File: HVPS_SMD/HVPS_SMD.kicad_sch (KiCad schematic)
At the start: 17 parts

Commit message: Shrink
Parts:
- C1: value (none) -> 100uF; footprint (none) -> lib_fp:C_1210
- C2: value (none) -> 0.01uF
- C3: value (none) -> 0.22uF; footprint (none) -> lib_fp:C_1210
- Cc1: value (none) -> 22nF
- Cs1: value (none) -> 360pF
- J1, J2: value (none) -> CONN_01X02
- Q1: value (none) -> AO4294
- R1: footprint (none) -> lib_fp:R_0805
- Rc1: value (none) -> 4.7k; footprint (none) -> lib_fp:R_0805
- Rf1: value (none) -> 47k; footprint (none) -> lib_fp:R_0805
- Rs1: value (none) -> 249; footprint (none) -> lib_fp:R_1206
- Rs2: footprint (none) -> Resistor_SMD:R_1206_3216Metric
- T1: value (none) -> MagTop-HVSMPS; footprint (none) -> lib_fp:nixiemisc-WE-FLEX_ER11_5
- U1: value (none) -> LM3478SOIC8
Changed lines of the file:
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@@
       (effects (font (size 1.143 1.143)) (justify left bottom))
     )
-    (property "Value" "" (id 1) (at 111.76 101.6 0)
+    (property "Value" "LM3478SOIC8" (id 1) (at 111.76 101.6 0)
       (effects (font (size 1.143 1.143)) (justify left bottom))
     )
@@
       (effects (font (size 1.143 1.143)) (justify left bottom))
     )
-    (property "Value" "" (id 1) (at 146.05 85.09 0)
+    (property "Value" "AO4294" (id 1) (at 146.05 85.09 0)
       (effects (font (size 1.143 1.143)) (justify left bottom))
     )
@@
       (effects (font (size 1.27 1.27)) hide)
     )
-    (property "Value" "" (id 1) (at 109.22 113.03 0))
+    (property "Value" "GND" (id 1) (at 109.22 113.03 0))
     (property "Footprint" "" (id 2) (at 109.22 109.22 0))
     (property "Datasheet" "" (id 3) (at 109.22 109.22 0))
@@
       (effects (font (size 1.27 1.27)) hide)
     )
-    (property "Value" "" (id 1) (at 101.6 113.03 0))
+    (property "Value" "GND" (id 1) (at 101.6 113.03 0))
     (property "Footprint" "" (id 2) (at 101.6 109.22 0))
     (property "Datasheet" "" (id 3) (at 101.6 109.22 0))
@@
       (effects (font (size 1.27 1.27)) hide)
     )
-    (property "Value" "" (id 1) (at 143.51 113.03 0))
+    (property "Value" "GND" (id 1) (at 143.51 113.03 0))
     (property "Footprint" "" (id 2) (at 143.51 109.22 0))
     (property "Datasheet" "" (id 3) (at 143.51 109.22 0))
@@
       (effects (font (size 1.27 1.27)) (justify left))
     )
-    (property "Footprint" "" (id 2) (at 143.51 102.87 0)
-      (effects (font (size 1.27 1.27)) hide)
-    )
-    (property "Datasheet" "" (id 3) (at 143.51 102.87 0)
+    (property "Footprint" "Resistor_SMD:R_1206_3216Metric" (id 2) (at 143.51 102.87 0)
+      (effects (font (size 1.27 1.27)) hide)
+    )
+    (property "Datasheet" "C327069" (id 3) (at 143.51 102.87 0)
       (effects (font (size 1.27 1.27)) hide)
     )
@@
       (effects (font (size 1.27 1.27)) (justify left))
     )
-    (property "Value" "" (id 1) (at 137.414 104.902 0)
+    (property "Value" "0.01uF" (id 1) (at 137.414 104.902 0)
       (effects (font (size 1.27 1.27)) (justify left))
     )
@@
       (effects (font (size 1.27 1.27)) hide)
     )
-    (property "Value" "" (id 1) (at 137.16 113.03 0))
+    (property "Value" "GND" (id 1) (at 137.16 113.03 0))
     (property "Footprint" "" (id 2) (at 137.16 109.22 0))
     (property "Datasheet" "" (id 3) (at 137.16 109.22 0))
@@
       (effects (font (size 1.27 1.27)) (justify left))
     )
-    (property "Value" "" (id 1) (at 87.884 101.092 0)
+    (property "Value" "22nF" (id 1) (at 87.884 101.092 0)
       (effects (font (size 1.27 1.27)) (justify left))
     )
@@
       (effects (font (size 1.27 1.27)) (justify left))
     )
-    (property "Value" "" (id 1) (at 88.392 106.426 0)
-      (effects (font (size 1.27 1.27)) (justify left))
-    )
-    (property "Footprint" "" (id 2) (at 87.63 105.41 0)
+    (property "Value" "4.7k" (id 1) (at 88.392 106.426 0)
+      (effects (font (size 1.27 1.27)) (justify left))
+    )
+    (property "Footprint" "lib_fp:R_0805" (id 2) (at 87.63 105.41 0)
       (effects (font (size 1.27 1.27)) hide)
     )
@@
       (effects (font (size 1.27 1.27)) hide)
     )
-    (property "Value" "" (id 1) (at 87.63 113.03 0))
+    (property "Value" "GND" (id 1) (at 87.63 113.03 0))
     (property "Footprint" "" (id 2) (at 87.63 109.22 0))
     (property "Datasheet" "" (id 3) (at 87.63 109.22 0))
@@
       (effects (font (size 1.27 1.27)) (justify left))
     )
-    (property "Value" "" (id 1) (at 192.024 42.672 0)
-      (effects (font (size 1.27 1.27)) (justify left))
-    )
-    (property "Footprint" "" (id 2) (at 191.77 40.64 0)
+    (property "Value" "0.22uF" (id 1) (at 192.024 42.672 0)
+      (effects (font (size 1.27 1.27)) (justify left))
+    )
+    (property "Footprint" "lib_fp:C_1210" (id 2) (at 191.77 40.64 0)
       (effects (font (size 1.27 1.27)) hide)
     )
@@
       (effects (font (size 1.27 1.27)) hide)
     )
-    (property "Value" "" (id 1) (at 191.77 62.23 0))
+    (property "Value" "GND" (id 1) (at 191.77 62.23 0))
     (property "Footprint" "" (id 2) (at 191.77 58.42 0))
     (property "Datasheet" "" (id 3) (at 191.77 58.42 0))
@@
       (effects (font (size 1.27 1.27)) (justify left))
     )
-    (property "Value" "" (id 1) (at 88.646 85.598 0)
-      (effects (font (size 1.27 1.27)) (justify left))
-    )
-    (property "Footprint" "" (id 2) (at 87.63 86.36 0)
+    (property "Value" "47k" (id 1) (at 88.646 85.598 0)
+      (effects (font (size 1.27 1.27)) (justify left))
+    )
+    (property "Footprint" "lib_fp:R_0805" (id 2) (at 87.63 86.36 0)
       (effects (font (size 1.27 1.27)) hide)
     )
@@
       (effects (font (size 1.27 1.27)) hide)
     )
-    (property "Value" "" (id 1) (at 177.8 113.03 0))
+    (property "Value" "GND" (id 1) (at 177.8 113.03 0))
     (property "Footprint" "" (id 2) (at 177.8 109.22 0))
     (property "Datasheet" "" (id 3) (at 177.8 109.22 0))
@@
       (effects (font (size 1.27 1.27)) (justify left))
     )
-    (property "Value" "" (id 1) (at 131.572 70.866 0)
-      (effects (font (size 1.27 1.27)) (justify left))
-    )
-    (property "Footprint" "" (id 2) (at 130.81 69.85 0)
+    (property "Value" "249" (id 1) (at 131.572 70.866 0)
+      (effects (font (size 1.27 1.27)) (justify left))
+    )
+    (property "Footprint" "lib_fp:R_1206" (id 2) (at 130.81 69.85 0)
       (effects (font (size 1.27 1.27)) hide)
     )
@@
       (effects (font (size 1.27 1.27)) (justify left))
     )
-    (property "Value" "" (id 1) (at 131.064 62.992 0)
+    (property "Value" "360pF" (id 1) (at 131.064 62.992 0)
       (effects (font (size 1.27 1.27)) (justify left))
     )
@@
       (effects (font (size 1.27 1.27)) (justify left))
     )
-    (property "Value" "" (id 1) (at 69.215 90.17 0)
-      (effects (font (size 1.27 1.27)) (justify left))
-    )
-    (property "Footprint" "" (id 2) (at 68.58 87.63 0)
+    (property "Value" "100uF" (id 1) (at 69.215 90.17 0)
+      (effects (font (size 1.27 1.27)) (justify left))
+    )
+    (property "Footprint" "lib_fp:C_1210" (id 2) (at 68.58 87.63 0)
       (effects (font (size 1.27 1.27)) hide)
     )
@@
       (effects (font (size 1.27 1.27)) hide)
     )
-    (property "Value" "" (id 1) (at 68.58 113.03 0))
+    (property "Value" "GND" (id 1) (at 68.58 113.03 0))
     (property "Footprint" "" (id 2) (at 68.58 109.22 0))
     (property "Datasheet" "" (id 3) (at 68.58 109.22 0))
@@
     (in_bom yes) (on_board yes)
     (property "Reference" "J2" (id 0) (at 43.18 63.5 0))
-    (property "Value" "" (id 1) (at 40.64 59.69 90))
+    (property "Value" "CONN_01X02" (id 1) (at 40.64 59.69 90))
     (property "Footprint" "NixieClockMaster:Header_MA02-Edge" (id 2) (at 43.18 59.69 0)
       (effects (font (size 1.27 1.27)) hide)
@@
       (effects (font (size 1.27 1.27)) hide)
     )
-    (property "Value" "" (id 1) (at 43.18 99.06 0))
+    (property "Value" "GND" (id 1) (at 43.18 99.06 0))
     (property "Footprint" "" (id 2) (at 43.18 95.25 0))
     (property "Datasheet" "" (id 3) (at 43.18 95.25 0))
@@
       (effects (font (size 1.27 1.27)) hide)
     )
-    (property "Value" "" (id 1) (at 49.53 99.06 0))
+    (property "Value" "VCC" (id 1) (at 49.53 99.06 0))
     (property "Footprint" "" (id 2) (at 49.53 95.25 0))
     (property "Datasheet" "" (id 3) (at 49.53 95.25 0))
@@
       (effects (font (size 1.27 1.27)) hide)
     )
-    (property "Value" "" (id 1) (at 55.88 97.536 0))
+    (property "Value" "HT" (id 1) (at 55.88 97.536 0))
     (property "Footprint" "" (id 2) (at 55.88 95.25 0))
     (property "Datasheet" "" (id 3) (at 55.88 95.25 0))
@@
       (effects (font (size 1.27 1.27)) (justify left))
     )
-    (property "Footprint" "" (id 2) (at 177.8 76.2 0)
+    (property "Footprint" "lib_fp:R_0805" (id 2) (at 177.8 76.2 0)
       (effects (font (size 1.27 1.27)) hide)
     )
@@
     (in_bom yes) (on_board yes)
     (property "Reference" "J1" (id 0) (at 43.18 46.99 0))
-    (property "Value" "" (id 1) (at 40.64 43.18 90))
+    (property "Value" "CONN_01X02" (id 1) (at 40.64 43.18 90))
     (property "Footprint" "NixieClockMaster:Header_MA02-Edge" (id 2) (at 43.18 43.18 0)
       (effects (font (size 1.27 1.27)) hide)
@@
     (in_bom yes) (on_board yes)
     (property "Reference" "#FLG0101" (id 0) (at 109.22 42.799 0))
-    (property "Value" "" (id 1) (at 109.22 45.1104 0))
+    (property "Value" "PWR_FLAG" (id 1) (at 109.22 45.1104 0))
     (property "Footprint" "" (id 2) (at 109.22 49.53 0)
       (effects (font (size 1.27 1.27)) hide)
@@
     (in_bom yes) (on_board yes)
     (property "Reference" "#FLG0102" (id 0) (at 170.18 96.139 0))
-    (property "Value" "" (id 1) (at 170.18 98.4504 0))
+    (property "Value" "PWR_FLAG" (id 1) (at 170.18 98.4504 0))
     (property "Footprint" "" (id 2) (at 170.18 102.87 0)
       (effects (font (size 1.27 1.27)) hide)
@@
       (effects (font (size 1.27 1.27)) hide)
     )
-    (property "Value" "" (id 1) (at 205.74 23.5204 0))
+    (property "Value" "PWR_FLAG" (id 1) (at 205.74 23.5204 0))
     (property "Footprint" "" (id 2) (at 205.74 27.94 0)
       (effects (font (size 1.27 1.27)) hide)
@@
       (effects (font (size 1.143 1.143)))
     )
-    (property "Value" "" (id 1) (at 168.9862 45.339 0)
+    (property "Value" "MagTop-HVSMPS" (id 1) (at 168.9862 45.339 0)
       (effects (font (size 1.143 1.143)))
     )
-    (property "Footprint" "" (id 2) (at 169.672 54.61 0)
+    (property "Footprint" "lib_fp:nixiemisc-WE-FLEX_ER11_5" (id 2) (at 169.672 54.61 0)
       (effects (font (size 0.508 0.508)) hide)
     )
@@
     )
     (path "/00000000-0000-0000-0000-000059c9976f"
-      (reference "Rs2") (unit 1) (value "0.062") (footprint "lib_fp:R_2010")
+      (reference "Rs2") (unit 1) (value "0.062") (footprint "Resistor_SMD:R_1206_3216Metric")
     )
     (path "/00000000-0000-0000-0000-00005ee051e4"

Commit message: Connectors for pin receptacles
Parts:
- J1, J2: footprint NixieClockMaster:Header_MA02-Edge -> NixieClockMaster:Header_MA02-Edge-3.2
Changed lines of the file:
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@@
     (property "Reference" "J2" (id 0) (at 43.18 63.5 0))
     (property "Value" "CONN_01X02" (id 1) (at 40.64 59.69 90))
-    (property "Footprint" "NixieClockMaster:Header_MA02-Edge" (id 2) (at 43.18 59.69 0)
+    (property "Footprint" "NixieClockMaster:Header_MA02-Edge-3.2" (id 2) (at 43.18 59.69 0)
       (effects (font (size 1.27 1.27)) hide)
     )
@@
     (property "Reference" "J1" (id 0) (at 43.18 46.99 0))
     (property "Value" "CONN_01X02" (id 1) (at 40.64 43.18 90))
-    (property "Footprint" "NixieClockMaster:Header_MA02-Edge" (id 2) (at 43.18 43.18 0)
+    (property "Footprint" "NixieClockMaster:Header_MA02-Edge-3.2" (id 2) (at 43.18 43.18 0)
       (effects (font (size 1.27 1.27)) hide)
     )
@@
     )
     (path "/00000000-0000-0000-0000-000059cc5eb0"
-      (reference "J1") (unit 1) (value "CONN_01X02") (footprint "NixieClockMaster:Header_MA02-Edge")
+      (reference "J1") (unit 1) (value "CONN_01X02") (footprint "NixieClockMaster:Header_MA02-Edge-3.2")
     )
     (path "/00000000-0000-0000-0000-000059c9bab8"
-      (reference "J2") (unit 1) (value "CONN_01X02") (footprint "NixieClockMaster:Header_MA02-Edge")
+      (reference "J2") (unit 1) (value "CONN_01X02") (footprint "NixieClockMaster:Header_MA02-Edge-3.2")
     )
     (path "/00000000-0000-0000-0000-000059c9950d"

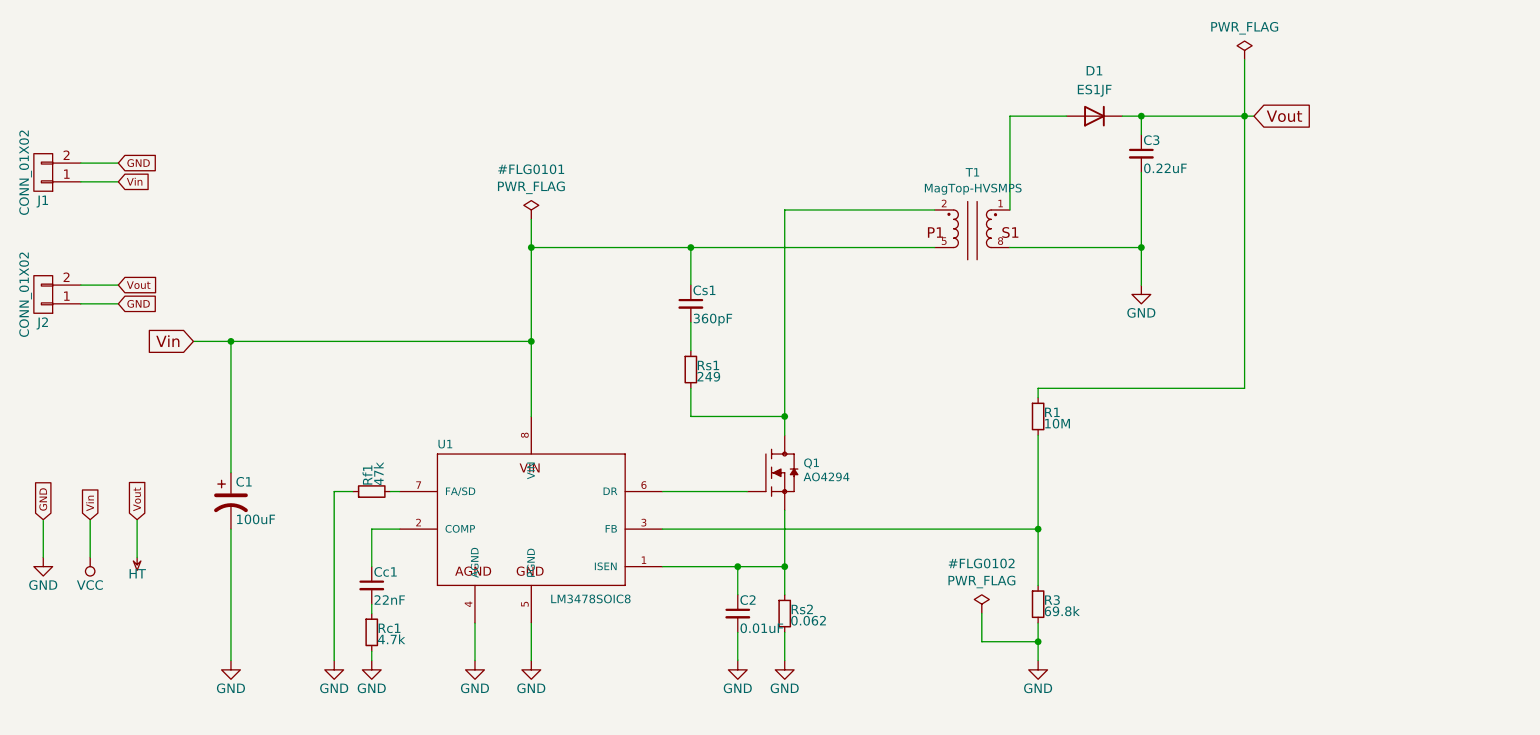
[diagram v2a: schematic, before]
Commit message: Add fiducials and external control options
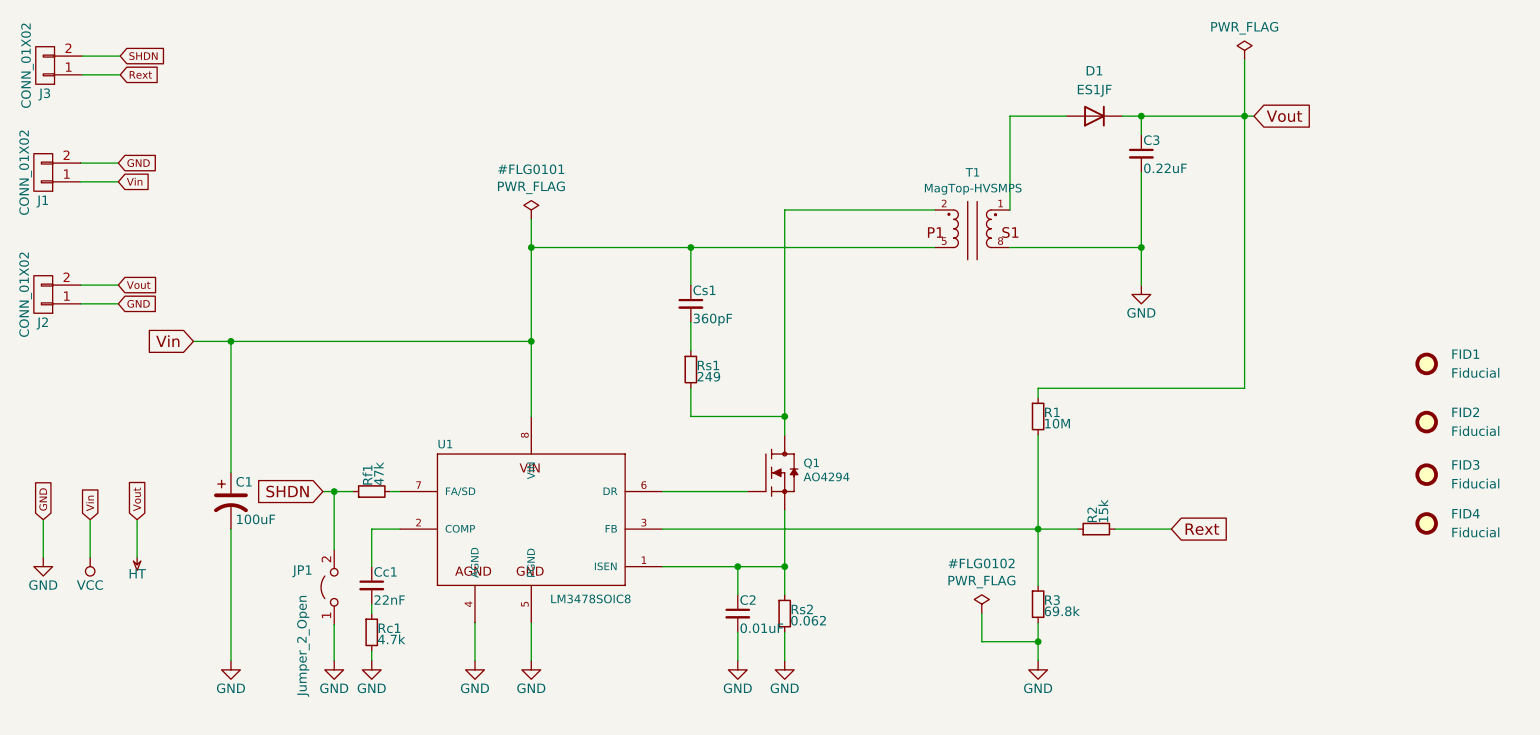
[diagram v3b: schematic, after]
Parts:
- added FID1, FID2, FID3, FID4: Fiducial, Fiducial:Fiducial_0.75mm_Mask1.5mm, symbol Mechanical:Fiducial
- added J3: CONN_01X02, NixieClockMaster:Header_MA02-Edge-3.2, symbol HVPS_SMD:CONN_01X02
- added JP1: Jumper_2_Open, NixieClockMaster:SolderJumper-2_P1.3mm_Open_Pad1.0x1.5mm_NoCtYd, symbol NixieClockMaster:Jumper_2_Open
- added R2: 15k, lib_fp:R_0805, symbol HVPS_SMD:R_Small
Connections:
- net GND: now also JP1.1 (A); no longer Rf1.1
- net at R1.2, R3.1, U1.3 (FB): now also R2.1
- new net Rext: J3.1 (P1), R2.2
- new net SHDN: J3.2 (P2), JP1.2 (B), Rf1.1

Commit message: Title blocks
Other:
- title: (none) -> Nixie High Voltage Switch Mode Power Supply
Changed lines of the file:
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@@
 (kicad_sch (version 20211123) (generator eeschema)
-  (paper "USLetter")
+  (paper "A4")
+  (title_block
+    (title "Nixie High Voltage Switch Mode Power Supply")
+    (date "2024-09-24")
+  )
   (junction (at 191.77 53.34) (diameter 0) (color 0 0 0 0)
   )

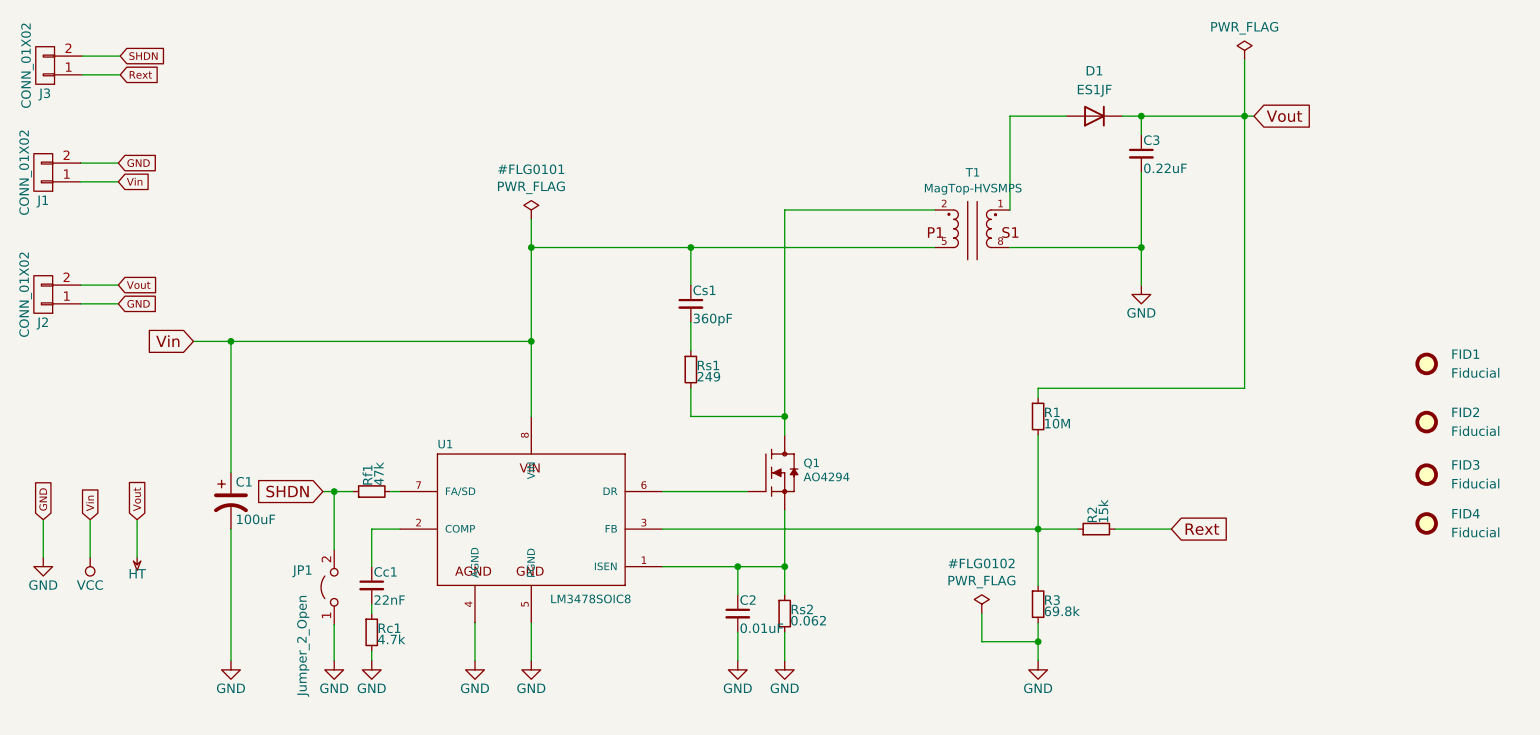
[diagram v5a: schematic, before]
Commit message: Update Kicad version
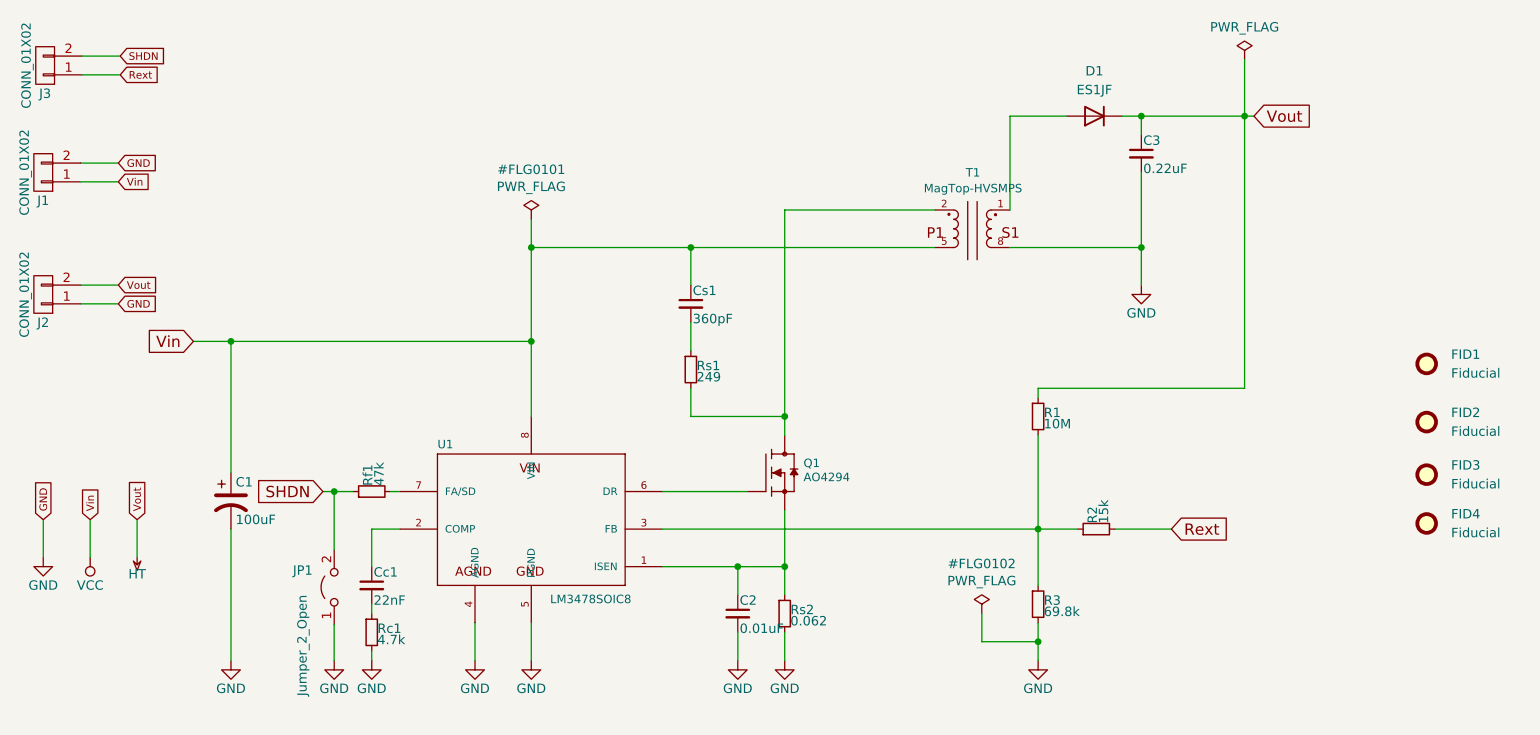
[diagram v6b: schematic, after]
